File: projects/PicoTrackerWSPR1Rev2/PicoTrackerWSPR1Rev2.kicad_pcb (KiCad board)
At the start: 2 copper layers, 51 parts, among them J1 Conn_01x02, M1 SIP32431DR3-T1GE3, M2 SIP32431DR3-T1GE3, M3 UBLOX_NEO-6, M4 SI5351A, U1 ATMEGA328P-AU, Y1 CRYSTAL_ABM8G

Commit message: KiCad PicoTrackerWSPR1Rev2 complete
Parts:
- added CONN25: TAP, Socket_Strips:Socket_Strip_Straight_1x01_Pitch2.54mm, F.Cu at (116.1, 72.1)
- CONN10: value SCL_TAP -> SCL
- CONN11: value MISO -> SPI_MISO
- CONN12: value SCK -> SPI_SCK
- CONN13: value RESET -> SPI_RESET
- CONN15: value MOSI -> SPI_MOSI
- CONN17: value GPS_TX -> GTX
- CONN18: value GPS_RX -> GRX
- CONN19: value SIG_A -> A
- CONN20: value SIG_B -> B
- CONN3: value VCC -> BATT
- CONN5: value MCU_RX -> ARX
- CONN6: value MCU_TX -> ATX
- CONN8: value TAP -> VCC
- CONN9: value SDA_TAP -> SDA
- moved CONN20 62.4 mm to (126.1, 72.1), turned to 90 degrees
- moved CONN4 59.9 mm to (116.1, 75.7), turned to 90 degrees
- moved CONN19 55.6 mm to (121.0, 72.1), turned to 90 degrees
- moved CONN8 55.4 mm to (111.0, 68.6), turned to 90 degrees
- moved CONN10 53.7 mm to (126.1, 79.2), turned to 90 degrees
- moved CONN3 53.3 mm to (111.0, 75.7), turned to 90 degrees
- moved CONN7 51.1 mm to (111.0, 72.1), turned to 90 degrees
- moved CONN6 49.4 mm to (126.1, 75.7), turned to 90 degrees
- moved CONN9 47.2 mm to (121.0, 79.2), turned to 90 degrees
- moved CONN5 42.6 mm to (121.0, 75.7), turned to 90 degrees
- moved CONN17 40.6 mm to (126.1, 82.8), turned to 90 degrees
- moved CONN18 34.0 mm to (121.0, 82.8), turned to 90 degrees
- moved CONN13 22.5 mm to (111.0, 80.0), turned to 270 degrees
- moved CONN11 22.0 mm to (116.1, 80.0), turned to 270 degrees
- moved CONN12 22.0 mm to (113.5, 80.0), turned to 270 degrees
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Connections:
- CONN3 pad 1: VCC -> VBATT
- CONN7 pad 1: VCC -> VBATT
- CONN8 pad 1: GND -> VCC
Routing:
- net GND: track 3.57 -> 95.6 mm, vias 1 -> 8
- net VBATT: track 17.1 -> 89.1 mm, vias 2 -> 5
- net SCL: track 0.00 -> 68.4 mm, vias 0 -> 9
- net SDA: track 0.00 -> 58.5 mm, vias 0 -> 7
- net SIG_A: track 0.00 -> 43.8 mm, vias 0 -> 3
- net SPI_RESET: track 0.00 -> 42.9 mm, vias 0 -> 5
- net SIG_B: track 0.00 -> 42.7 mm, vias 0 -> 6
- net SER_TXD: track 0.00 -> 40.9 mm, vias 0 -> 6
- net SER_RXD: track 0.00 -> 33.6 mm, vias 0 -> 6
- net GPS_SER_OUT: track 50.4 -> 78.4 mm, vias 2 -> 4
- net VCC: track 84.3 -> 111.6 mm, vias 2 -> 11
- net SPI_MISO: track 0.00 -> 26.2 mm, vias 0 -> 3
- net SPI_MOSI: track 0.00 -> 26.0 mm, vias 0 -> 3
- net REG_PS_CTL: track 0.00 -> 21.9 mm, vias 0 -> 4
- net SPI_SCK: track 0.00 -> 21.4 mm, vias 0 -> 3
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- added copper zone on B.Cu, net GND
- added copper zone on F.Cu, net GND
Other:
- board outline added: 75.7 x 23.9 mm
- board text added: "10k"
- board text added: "2019-02-22 PicoTrackerWSPR1 Rev 2"
- board text added: "220"
- board text added: "AVR"
- board text added: "G"
- board text added: "GPS"
- board text added: "GPS Ant"
- board text added: "KD2KDD - douglas.malnati@gmail.com KN4IUD - mark.malnati@gmail.com"
- board text added: "LEDs"
- board text added: "Please contact if found!"
- board text added: "R"
- board text added: "SI5351A CLKGEN TX"
- board text added: "SIP32431 Load Sw"
- board text added: "WSPR Ant"
- board text added: "bat cut"

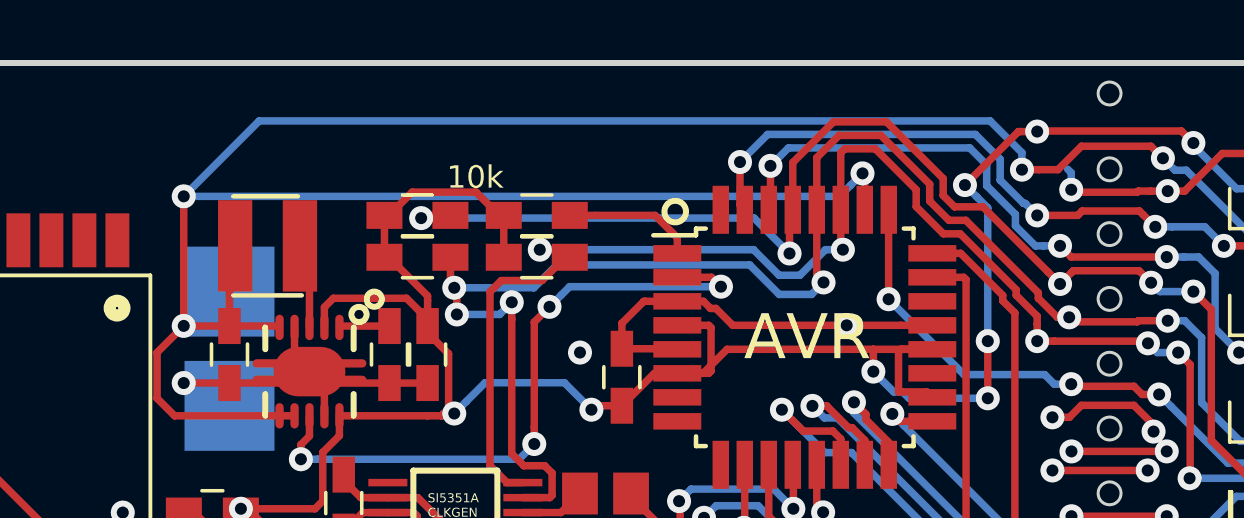
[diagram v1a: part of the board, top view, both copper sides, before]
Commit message: KiCad PicoTrackerWSPR1Rev2 added forgotten battery sense voltage divider
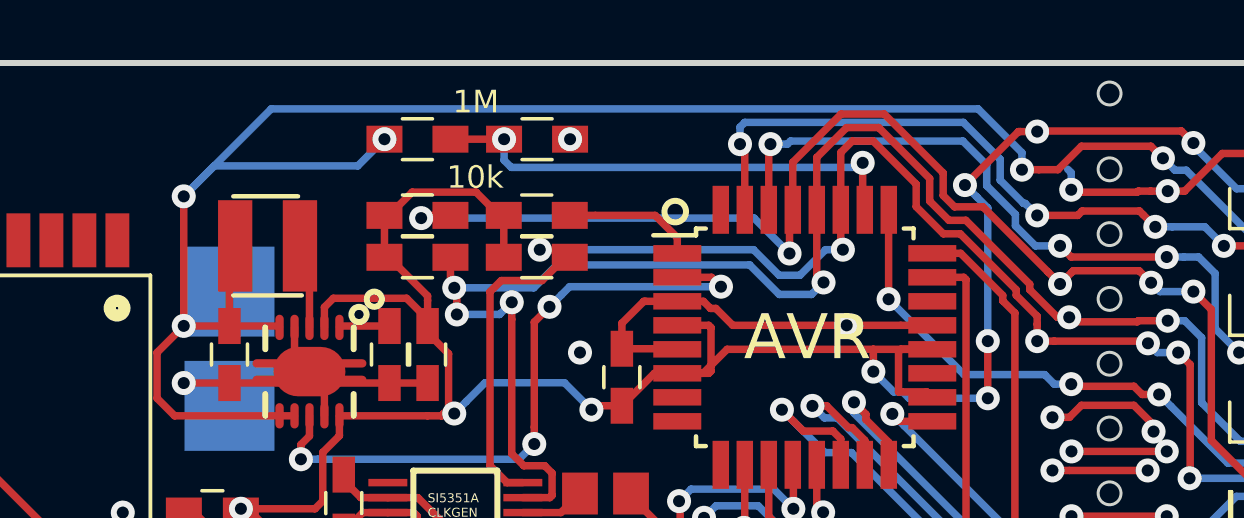
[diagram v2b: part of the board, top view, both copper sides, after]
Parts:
- added R7: 1M, Resistors_SMD:R_0603_HandSoldering, F.Cu at (82.6, 66.9)
- added R8: 1M, Resistors_SMD:R_0603_HandSoldering, F.Cu at (86.6, 66.9)
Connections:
- U1 pad 26: VBATT -> VBATT_SENSE
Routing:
- net VBATT: track 89.1 -> 72.7 mm
- net VBATT_SENSE: track 0.00 -> 16.2 mm, vias 0 -> 2
- net SER_TXD: track 40.9 -> 41.9 mm
- net SER_RXD: track 33.6 -> 34.2 mm
- net GND: vias 8 -> 9
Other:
- board text added: "1M"
- board text added: "2019-02-25 PicoTrackerWSPR1 Rev 2"
- board text removed: "2019-02-22 PicoTrackerWSPR1 Rev 2"
